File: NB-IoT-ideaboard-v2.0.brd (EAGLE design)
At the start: 72.7 x 54.1 mm, 98 parts, among them Q1 32.768kHz, Q2 8MHz, Q3 9013, Q4 9013, Q5 9013, U1 STM32F103RBT6, U2 MCP73831T-2ACI/OT, U3 AP2112-3.3, U4 PAM2401, U5 MICROSIM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

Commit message: Adds logos, mounting holes
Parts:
- added $H1, $H2, $H3, $H4: MOUNTINGHOLE3.0THIN, Adafruit SIM808 Breakout:MOUNTINGHOLE_3.0_PLATEDTHIN
- moved C1 9.06 mm to (162.6, 9.14), turned to 90 degrees
- moved USER 7.92 mm to (166.6, 12.2), turned to 270 degrees
- moved C9 6.90 mm to (170.8, 20.0)
- moved C20 6.52 mm to (219.5, 35.0), turned to 270 degrees
- moved R16 6.18 mm to (220.5, 31.1)
- moved R4 6.04 mm to (159.9, 13.2), turned to 90 degrees
- moved JP9 5.14 mm to (154.6, 29.3)
- moved R14 4.83 mm to (218.2, 39.4), turned to 270 degrees
- moved C17 4.34 mm to (222.9, 43.7)
- moved C16 4.34 mm to (222.9, 41.7)
- moved L2 4.24 mm to (223.1, 37.2)
- moved C19 4.14 mm to (222.9, 45.7)
- moved U3 4.14 mm to (222.9, 49.0)
- moved NET 3.45 mm to (211.9, 26.3)
- moved R3 3.17 mm to (162.6, 13.2), turned to 270 degrees
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- renumbered CONFIG to BOOT, JP1 to MODEMCTL
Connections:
- removed net VIN: JP5.6
- net PB12: now also JP9.8
- net PB13: now also JP9.7
- net PB15: now also JP9.5
- net PC6: no longer JP9.5
- net PC8: no longer JP9.7
- net PC9: no longer JP9.8
- net VBUS: now also JP5.6
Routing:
- net VBUS: track 30.3 -> 67.4 mm
- net N$22: track 4.54 -> 19.8 mm
- net PB15: track 0.00 -> 13.4 mm
- net PD2: track 12.4 -> 0.00 mm, vias 1 -> 0
- net N$19: track 13.7 -> 2.10 mm
- net PC6: track 11.6 -> 0.00 mm
- net PC12: track 11.5 -> 0.00 mm, vias 1 -> 0
- net PC11: track 11.0 -> 0.00 mm, vias 1 -> 0
- net JTDI: track 10.6 -> 0.00 mm, vias 1 -> 0
- net PC10: track 10.1 -> 0.00 mm, vias 1 -> 0
- net PC9: track 21.5 -> 11.9 mm
- net PB12: track 41.1 -> 50.5 mm
- net PB13: track 5.98 -> 13.9 mm
- net BC92_PWRKEY_MCU: track 30.7 -> 24.2 mm
- net PC13: track 38.5 -> 44.9 mm
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- removed copper zone on layer 1, net N$27
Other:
- board size 72.7 x 54.1 mm -> 74.8 x 54.5 mm
- board text added: "(BC92)"
- board text added: "A02"
- board text added: "A03"
- board text added: "A08"
- board text added: "A10"
- board text added: "A11"
- board text added: "A12"
- board text added: "A6"
- board text added: "A7"
- board text added: "A9"
- board text added: "ADC12 IN"
- board text added: "B03"
- board text added: "B05"
- board text added: "B12"
- board text added: "B13"
- board text added: "B14"
- board text added: "B15"
- board text added: "B6"
- board text added: "B8"
- board text added: "B9"
- board text added: "C0"
- board text added: "C1"
- board text added: "C7"
- board text added: "CAN1"
- board text added: "I2C1"
- board text added: "IDEABOARD V2.0"
- board text added: "MISO"
- board text added: "MOSI"
- board text added: "NRST"
- board text added: "NSS"
- board text added: "NSS1"
- board text added: "Quectel BC92"
- board text added: "RX2"
- board text added: "SCK"
- board text added: "SPI 1"
- board text added: "SPI 2"
- board text added: "STM32F103RBT6"
- board text added: "SWCLK"
- board text added: "SWDIO"
- board text added: "SWO"
- board text added: "TX2"
- board text added: "USART1"
- board text added: "VBUS"
- board text added: "VDDA"
- board text added: "WKUP"
- board text removed: "#"
- board text removed: "10"
- board text removed: "11"
- board text removed: "12"
- board text removed: "13"
- board text removed: "2"
- board text removed: "3"
- board text removed: "4"
- board text removed: "5"
- board text removed: "6"
- board text removed: "7"
- board text removed: "8"
- board text removed: "9"
- board text removed: "A2"
- board text removed: "A3"
- board text removed: "ANALOG IN"
- board text removed: "AREF"
- board text removed: "DIGITAL"
- board text removed: "RESET"
- board text removed: "STM32F103RBT6 Quectel BC92"
- board text removed: "USART2"
- board text removed: "VIN"
- board text removed: "Version 2.0"
- board text removed: "[#=PWM]"

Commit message: Minor changes
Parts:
- removed $H4: MOUNTINGHOLE3.0THIN, Adafruit SIM808 Breakout:MOUNTINGHOLE_3.0_PLATEDTHIN
- R1: value 1k -> 330R
- R13, R28: value 2.2k -> 2k2
- R19, R20, R26: value 4.7k -> 4k7
- R25: value 2.2k -> 0R
- R6: value 5.6k -> 5k7
- S1: device SparkFun-Electromechanical:SWITCH-SPDT-SMD -> SparkFun-Electromechanical:SWITCH-SPST-SMD-A
- moved $H1 1.18 mm to (217.4, 26.2)
- moved S1 0.91 mm to (224.1, 25.2)
- moved Q2 0.20 mm to (189.0, 26.7)
- renumbered ANT1 to RF_ANT
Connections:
- net +3V3: now also R1.2
- net +5V: no longer R1.2
- net PA4: now also CC1101.4
- net PB6: no longer CC1101.4
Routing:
- net PA4: track 99.7 -> 128.2 mm, vias 1 -> 6
- net PB6: track 58.6 -> 39.4 mm, vias 3 -> 2
- net +3V3: track 206.5 -> 212.9 mm
- net +5V: track 79.7 -> 75.5 mm
- net +4.1V: track 26.7 -> 23.0 mm
- net PC1: track 102.7 -> 104.2 mm
- net PC0: track 103.0 -> 104.5 mm
- net PB0: track 106.1 -> 107.6 mm
- net V+: track 76.0 -> 76.9 mm
- net JNTRST: track 50.4 -> 51.3 mm
- net NRST: track 69.6 -> 70.5 mm
- net PA8: track 39.0 -> 39.8 mm
- net PB12: track 50.5 -> 51.2 mm
- net PB5: track 52.3 -> 53.0 mm
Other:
- outline, holes or cut-outs redrawn
- board text added: "2020/11/01"
- board text added: "B04"
- board text added: "BOOT0"
- board text added: "BOOT1"
- board text removed: "2018/06/01"

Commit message: Adjust USB port
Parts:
- moved $H1 151.2 mm to (66.2, 27.8)
- moved BOOT 151.2 mm to (46.3, 20.9)
- moved C1 151.2 mm to (11.4, 10.8)
- moved C12 151.2 mm to (28.7, 17.8)
- moved C13 151.2 mm to (33.5, 17.8)
- moved C14 151.2 mm to (69.7, 17.1)
- moved C16 151.2 mm to (71.7, 43.3)
- moved C17 151.2 mm to (71.7, 45.3)
- moved C19 151.2 mm to (71.7, 47.3)
- moved C2 151.2 mm to (31.3, 31.6)
- moved C21 151.2 mm to (62.0, 38.4)
- moved C23 151.2 mm to (64.3, 10.1)
- moved C24 151.2 mm to (62.8, 45.7)
- moved C25 151.2 mm to (62.8, 41.0)
- moved C27 151.2 mm to (62.8, 50.6)
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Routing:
- net VBUS: track 67.4 -> 69.1 mm
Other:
- board text added: "Add ws2812 stitch check antenna trace"
- board text removed: "logos stitch check antenna trace"

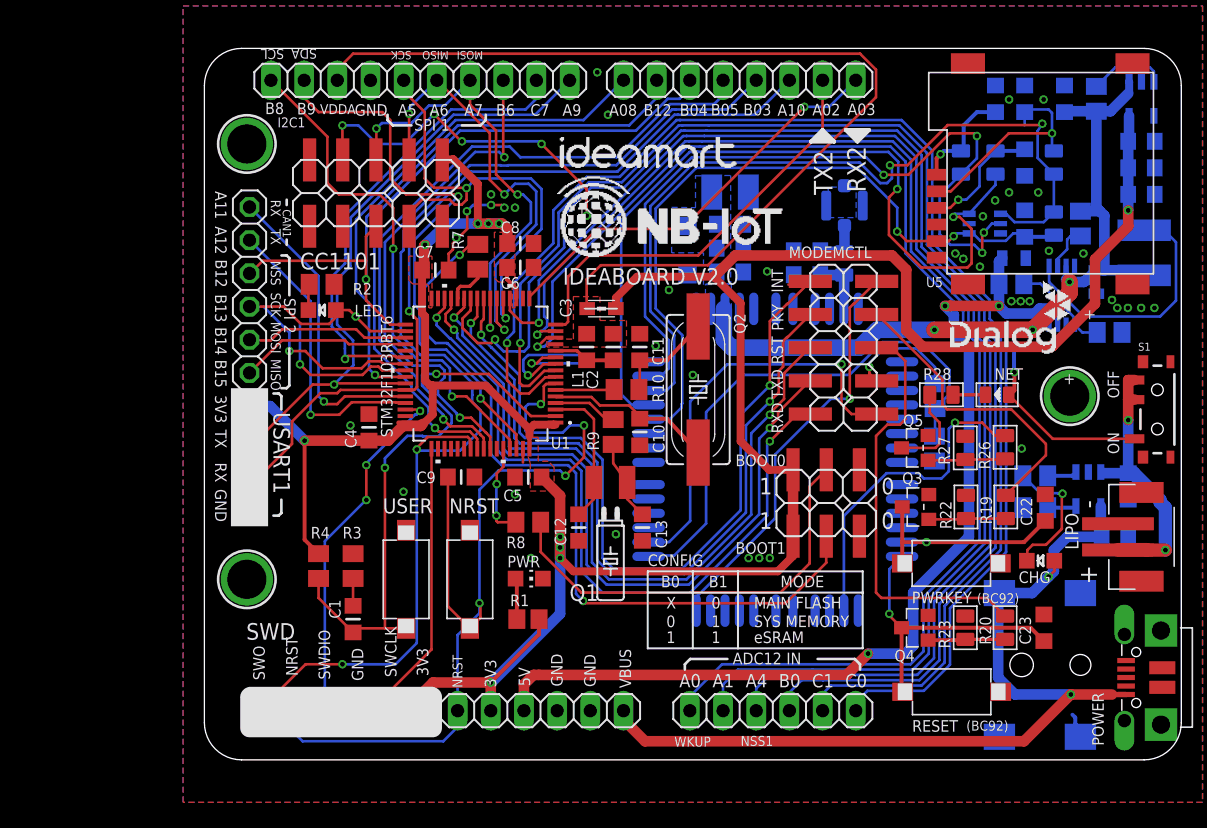
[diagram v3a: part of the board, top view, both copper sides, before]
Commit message: JLCPCB layout started
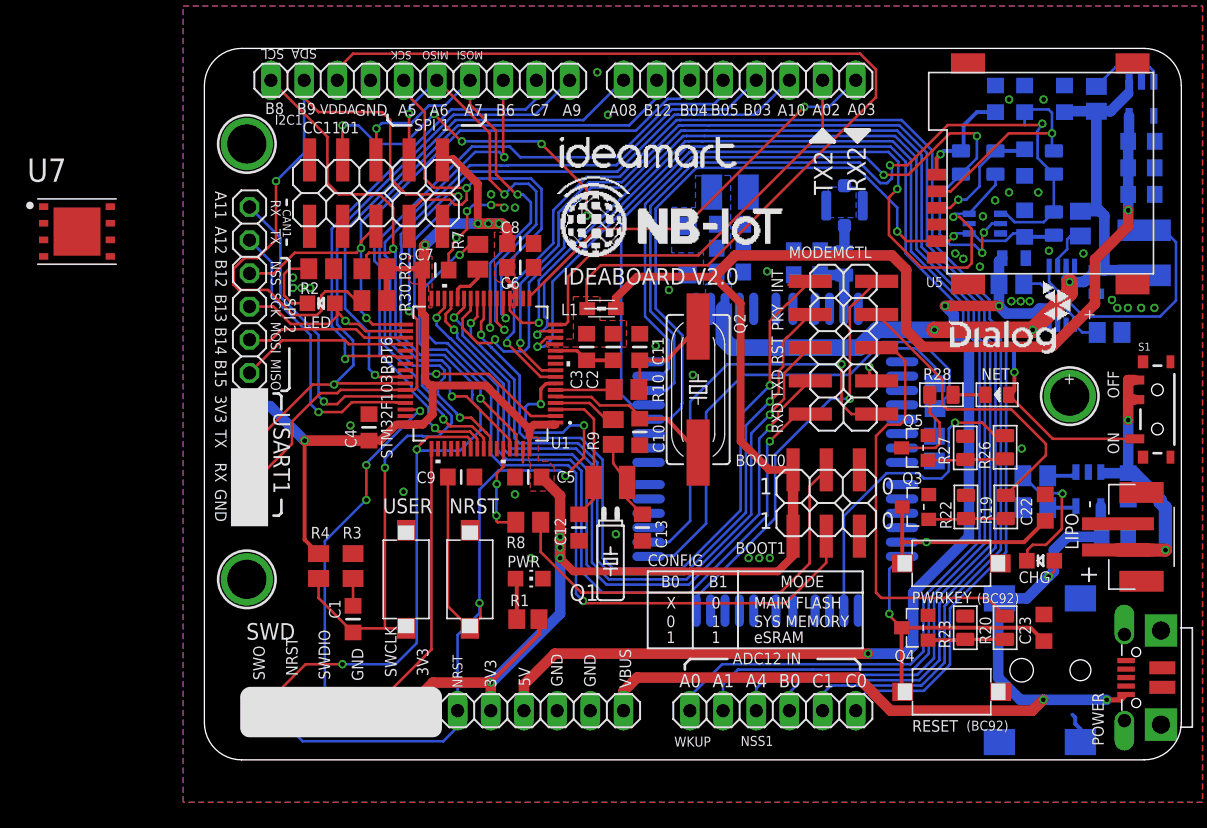
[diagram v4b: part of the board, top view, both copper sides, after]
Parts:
- added R29, R30: 5k7, resistor:M0805
- added U7: SIM-ST-MFF2, SIM-ST-MFF2:PSON127P500X600X82-9N
- R1, R2: value 330R -> 1k
- moved R2 1.19 mm to (8.94, 37.6)
- moved LED 0.53 mm to (8.94, 35.0)
- moved U$1 0.41 mm to (67.1, 6.86)
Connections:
- removed net PB7: U1.59
- removed net PB8: JP6.1, U1.61
- removed net PB9: JP6.2, U1.62
- removed net PC10: U1.51
- removed net PC11: U1.52
- removed net PC12: U1.53
- removed net PC2: U1.10
- removed net PC3: U1.11
- removed net PC6: U1.37
- removed net PC8: U1.39
- removed net PC9: U1.40
- removed net PD2: U1.54
- new net I2C1_SCL: JP6.1, R29.1, U1.61
- new net I2C1_SDA: JP6.2, R30.1, U1.62
- new net VCC: U7.8
- net +3V3: now also R29.2, R30.2
- net GND: now also U7.1
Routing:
- net I2C1_SDA: track 0.00 -> 74.7 mm, vias 0 -> 3
- net PB9: track 43.8 -> 0.00 mm, vias 2 -> 0
- net I2C1_SCL: track 0.00 -> 42.8 mm, vias 0 -> 2
- net PB8: track 39.4 -> 0.00 mm, vias 2 -> 0
- net PC8: track 14.0 -> 0.00 mm, vias 1 -> 0
- net PC9: track 11.9 -> 0.00 mm, vias 1 -> 0
- net PC2: track 8.30 -> 0.00 mm, vias 1 -> 0
- net PC3: track 5.71 -> 0.00 mm, vias 1 -> 0
- net +3V3: track 212.9 -> 218.2 mm
- net N$26: track 2.00 -> 5.74 mm
- net PC0: track 104.5 -> 101.8 mm
- net PC1: track 104.2 -> 101.7 mm
- net VBUS: track 69.1 -> 67.3 mm, vias 2 -> 3
- net PB13: track 13.9 -> 14.9 mm
- net PB12: track 51.2 -> 50.5 mm, vias 1 -> 2
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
